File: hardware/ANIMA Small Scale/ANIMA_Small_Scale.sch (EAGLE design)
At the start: 56 parts, among them J1 POW_CONNECTFEMALE-RA, Q1 MOSFET-PCHANNELSMD, Q2 MOSFET-PCHANNELSMD, Q3 MOSFET-PCHANNELSMD, U1 PIC32MX20FB-44PIN, U12 MICRO-SDCARDSOCKET, U2 TPS54040, U3 MEDIATEK-3329, U5 MMA8451Q, U6 MAG3110

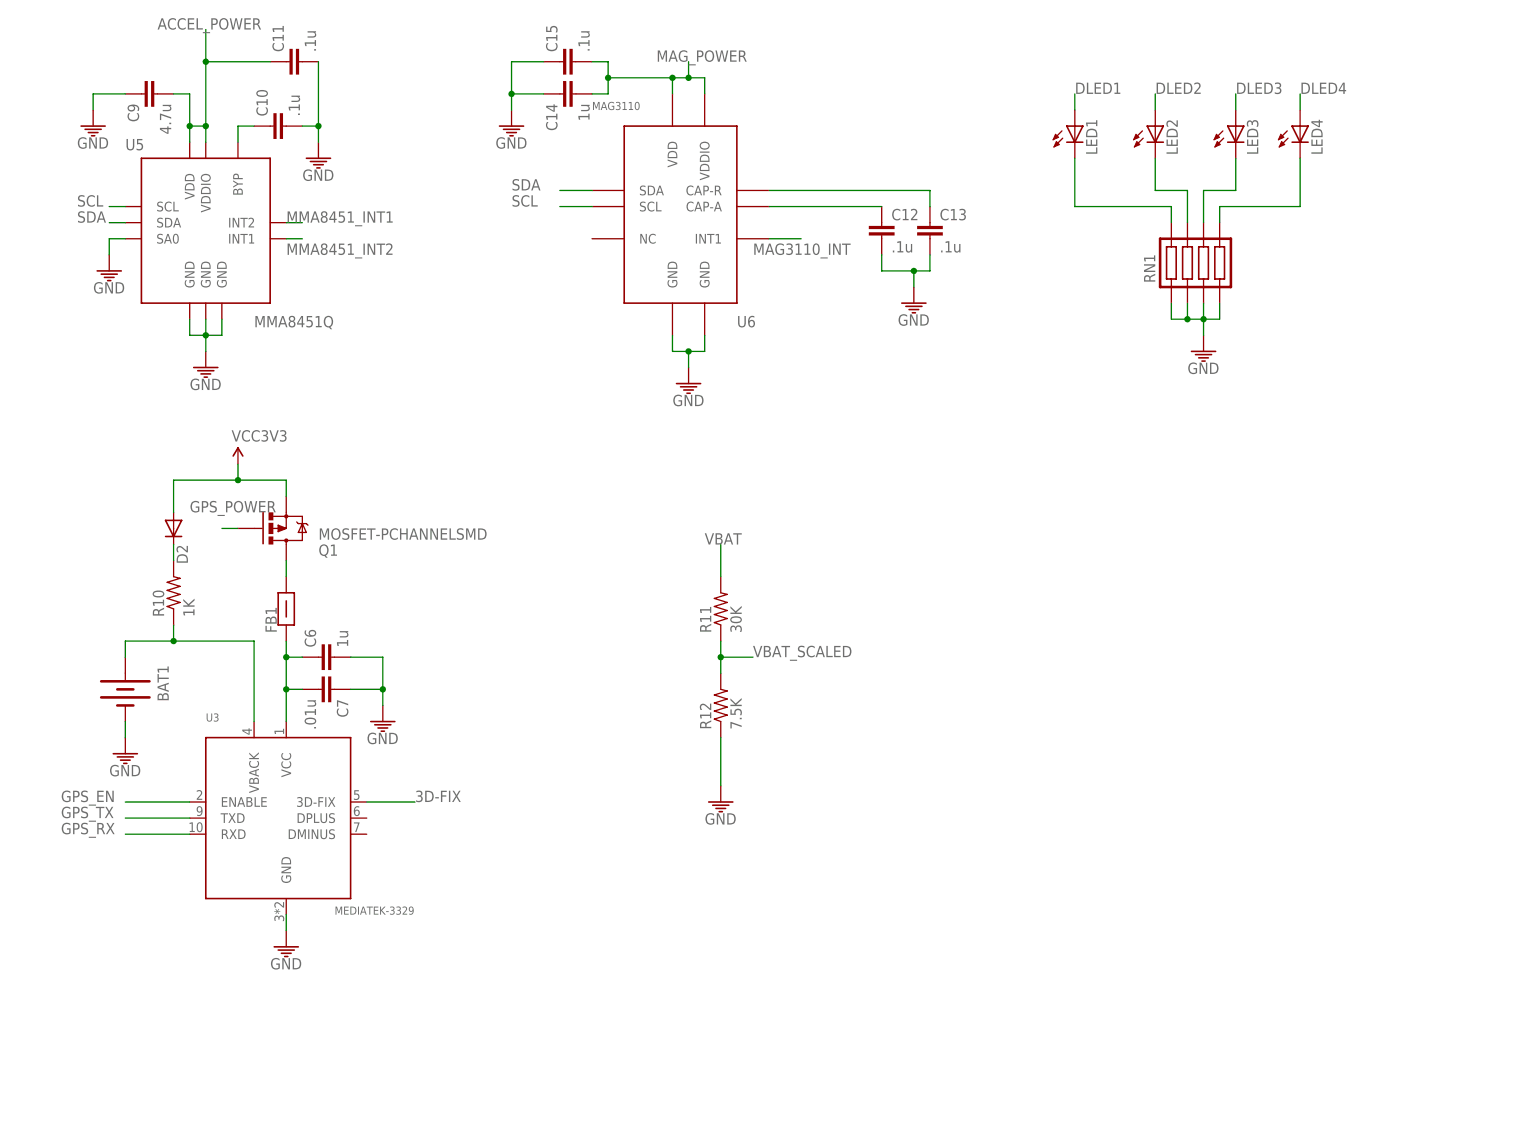
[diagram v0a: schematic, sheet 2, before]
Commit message: board renovations complete attempting to diagnose I2C again
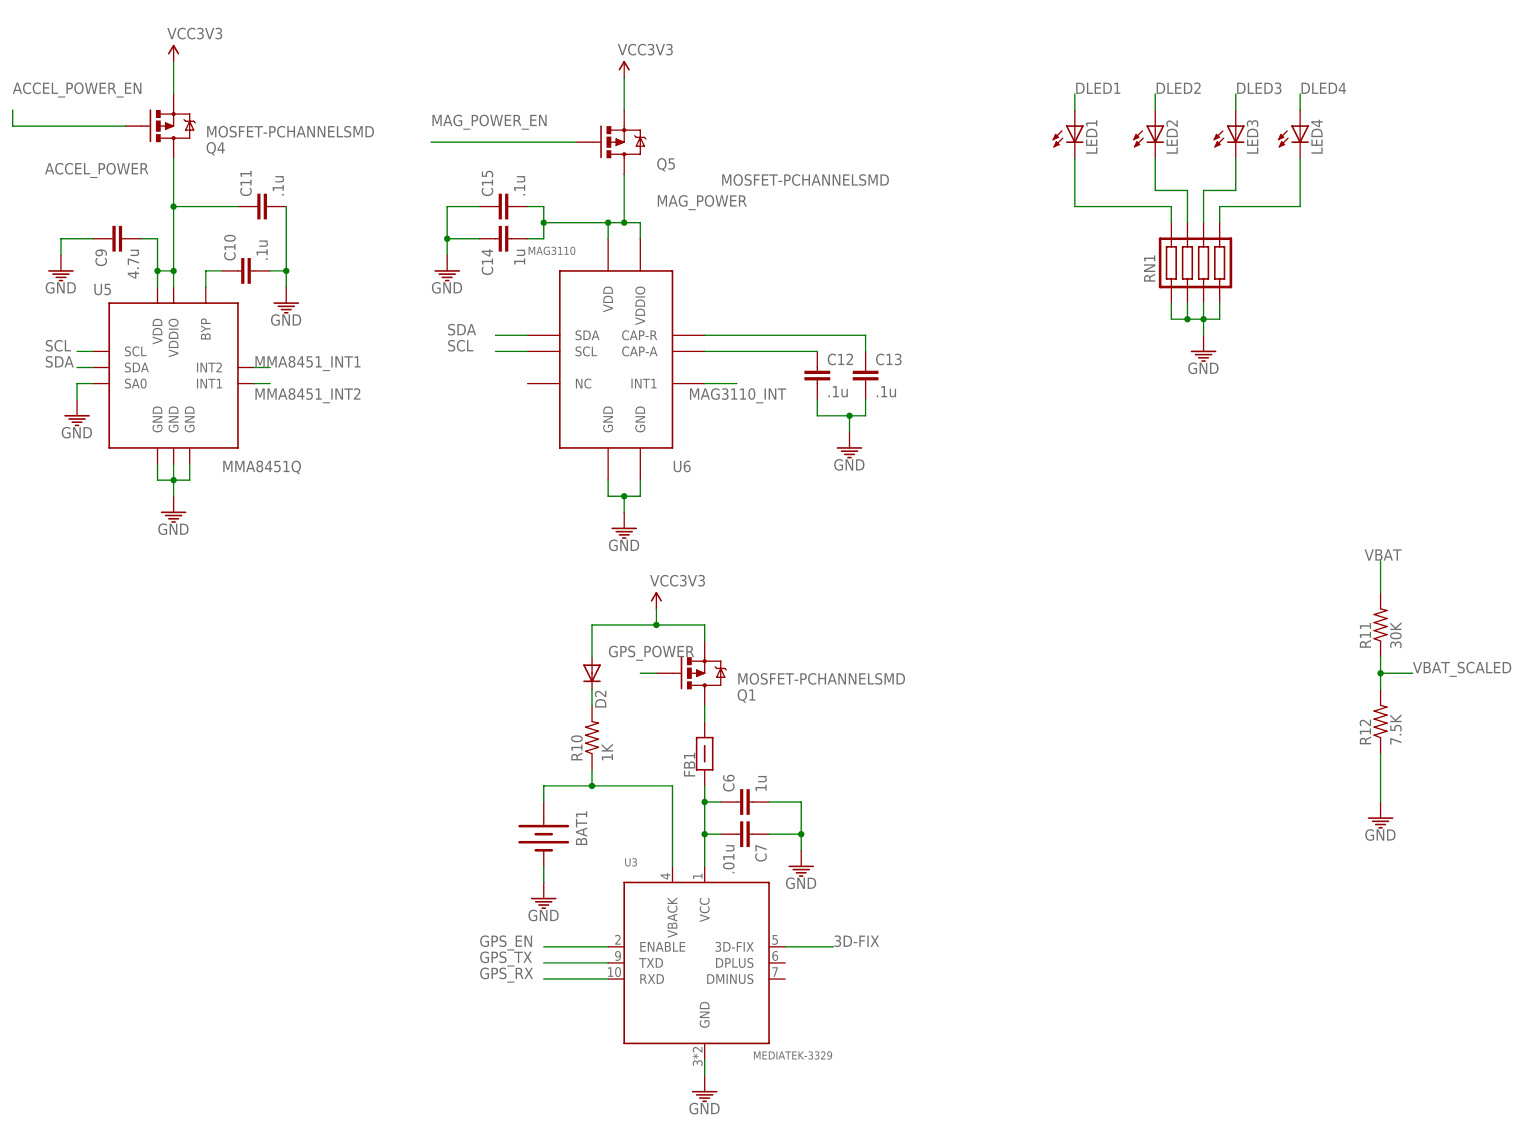
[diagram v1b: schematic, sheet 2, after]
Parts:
- added Q4, Q5, Q6: MOSFET-PCHANNELSMD, ANIMAlib:MOSFET-PCHANNELSMD
- added R14: 5.1K, ANIMAlib:RESISTOR0805-RES
- added U4: TC1047, ANIMAlib:TC1047
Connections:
- new net ACCEL_POWER_EN: Q4.G, U1PORTA.OSC1/CLKI/CN30/RA2
- new net I2C_POWER_EN: Q6.G, U1PORTC.AN6/RPC0/RC0
- new net MAG_POWER_EN: Q5.G, U1PORTA.OSC2/CLKO/CN29/RA3
- new net TEMPERATURE: U1PORTA.AN0/VREF+/CN2/RA0, U4.TEMP
- net ACCEL_POWER: now also Q4.D; no longer U1PORTA.OSC1/CLKI/CN30/RA2
- net CD1: now also R14.1
- net CD2: no longer U12.CD2
- net GND: now also U4.GND
- net GPS_POWER: now also U1PORTA.PGEC/CTED8/PMA7/RA7
- net I2C_POWER: now also Q6.D; no longer U1PORTC.AN6/RPC0/RC0
- net MAG_POWER: now also Q5.D; no longer U1PORTA.OSC2/CLKO/CN29/RA3
- net MMA8451_INT1: now also U1PORTC.AN8/RPC2/PMA2/RC2; no longer U1PORTC.AN7/RPC1/RC1
- net MMA8451_INT2: now also U1PORTC.AN7/RPC1/RC1; no longer U1PORTC.AN8/RPC2/PMA2/RC2
- net N$22: now also Q3.D; no longer Q3.S
- net PGEC: now also U1PORTB.PGEC1/AN3/RP1/CN5/RB1; no longer U1PORTA.AN1/VREF-/CN3/RA1
- net PGED: now also U1PORTB.PGED1/AN2/RP0/CN4/RB0; no longer U1PORTA.AN0/VREF+/CN2/RA0
- net SD_POWER_EN: now also U1PORTA.AN1/VREF-/CN3/RA1; no longer U1PORTB.PGED1/AN2/RP0/CN4/RB0
- net SS: now also U1PORTB.AN10//RP14/SCK1/RB14
- net VCC3V3: now also Q3.S, Q4.S, Q5.S, Q6.S, R14.2, U4.VCC; no longer Q3.D
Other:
- moved on the sheet: BAT1, C10, C11, C12, C13, C14, C15, C6, C7, C9, D2, FB1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
